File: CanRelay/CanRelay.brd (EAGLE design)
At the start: 93 x 65.5 mm, 21 parts

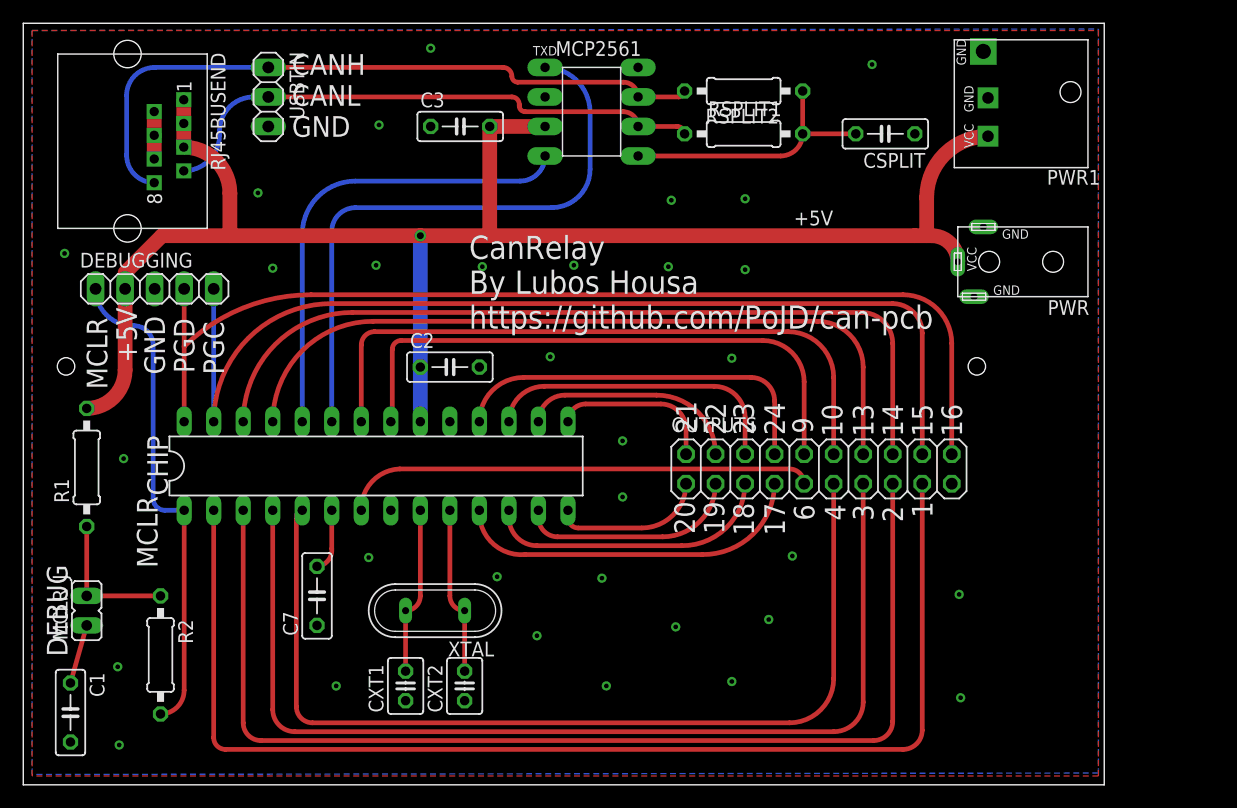
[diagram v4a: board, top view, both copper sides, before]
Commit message: #10 adding more missing GND vias to the board, running checks, adding  missing labels in schematic, done  #
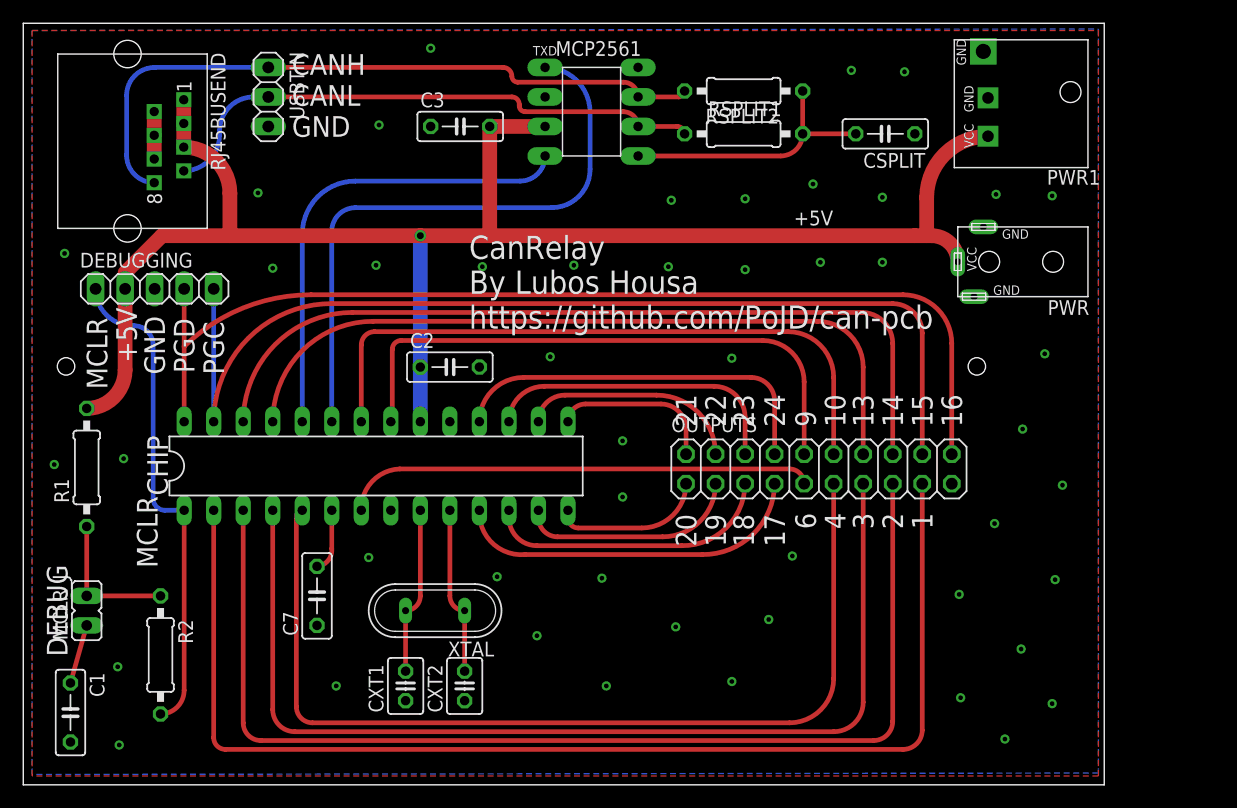
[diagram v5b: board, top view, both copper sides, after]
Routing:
- net GND: vias 32 -> 48
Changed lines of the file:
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@@
 <text x="17.272" y="35.306" size="1.778" layer="21" rot="R90">PGC</text>
 <text x="14.732" y="35.433" size="1.778" layer="21" rot="R90">PGD</text>
-<text x="57.912" y="30.226" size="1.778" layer="21" rot="R90">21</text>
-<text x="60.452" y="30.099" size="1.778" layer="21" rot="R90">22</text>
-<text x="62.865" y="30.099" size="1.778" layer="21" rot="R90">23</text>
-<text x="65.532" y="30.099" size="1.778" layer="21" rot="R90">24</text>
-<text x="67.945" y="30.226" size="1.778" layer="21" rot="R90">9</text>
-<text x="70.485" y="29.972" size="1.778" layer="21" rot="R90">10</text>
-<text x="73.152" y="29.972" size="1.778" layer="21" rot="R90">13</text>
-<text x="75.692" y="29.972" size="1.778" layer="21" rot="R90">14</text>
-<text x="78.232" y="29.972" size="1.778" layer="21" rot="R90">15</text>
-<text x="80.772" y="29.972" size="1.778" layer="21" rot="R90">16</text>
-<text x="57.785" y="21.59" size="1.778" layer="21" rot="R90">20</text>
-<text x="60.325" y="21.59" size="1.778" layer="21" rot="R90">19</text>
-<text x="62.865" y="21.463" size="1.778" layer="21" rot="R90">18</text>
-<text x="65.532" y="21.463" size="1.778" layer="21" rot="R90">17</text>
-<text x="68.072" y="22.733" size="1.778" layer="21" rot="R90">6</text>
-<text x="70.739" y="22.733" size="1.778" layer="21" rot="R90">4</text>
-<text x="73.152" y="22.733" size="1.778" layer="21" rot="R90">3</text>
-<text x="75.692" y="22.606" size="1.778" layer="21" rot="R90">2</text>
-<text x="78.232" y="22.987" size="1.778" layer="21" rot="R90">1</text>
+<text x="57.912" y="30.8" size="1.778" layer="21" rot="R90">21</text>
+<text x="60.452" y="30.8" size="1.778" layer="21" rot="R90">22</text>
+<text x="62.865" y="30.8" size="1.778" layer="21" rot="R90">23</text>
+<text x="65.532" y="30.8" size="1.778" layer="21" rot="R90">24</text>
+<text x="68.2" y="30.8" size="1.778" layer="21" rot="R90">9</text>
+<text x="70.739" y="30.8" size="1.778" layer="21" rot="R90">10</text>
+<text x="73.152" y="30.8" size="1.778" layer="21" rot="R90">13</text>
+<text x="75.692" y="30.8" size="1.778" layer="21" rot="R90">14</text>
+<text x="78.232" y="30.8" size="1.778" layer="21" rot="R90">15</text>
+<text x="80.772" y="30.8" size="1.778" layer="21" rot="R90">16</text>
+<text x="57.912" y="20.5" size="1.778" layer="21" rot="R90">20</text>
+<text x="60.452" y="20.5" size="1.778" layer="21" rot="R90">19</text>
+<text x="62.865" y="20.5" size="1.778" layer="21" rot="R90">18</text>
+<text x="65.532" y="20.5" size="1.778" layer="21" rot="R90">17</text>
+<text x="68.2" y="22" size="1.778" layer="21" rot="R90">6</text>
+<text x="70.739" y="22" size="1.778" layer="21" rot="R90">4</text>
+<text x="73.152" y="22" size="1.778" layer="21" rot="R90">3</text>
+<text x="75.692" y="22" size="1.778" layer="21" rot="R90">2</text>
+<text x="78.232" y="22" size="1.778" layer="21" rot="R90">1</text>
 <text x="11.557" y="18.669" size="1.778" layer="21" rot="R90">MCLR</text>
 <text x="3.81" y="11.049" size="1.778" layer="21" rot="R90">DEBUG</text>
@@
 <via x="3.556" y="45.72" extent="1-16" drill="0.4" shape="square"/>
 <via x="35.052" y="63.373" extent="1-16" drill="0.4" shape="square"/>
-<via x="73.025" y="61.976" extent="1-16" drill="0.4" shape="square"/>
+<via x="71.247" y="61.468" extent="1-16" drill="0.4" shape="square"/>
 <via x="8.636" y="28.067" extent="1-16" drill="0.4" shape="square"/>
 <via x="30.607" y="56.769" extent="1-16" drill="0.4" shape="square"/>
@@
 <wire x1="11.268" y1="57.922" x2="11.268" y2="55.882" width="1.27" layer="1"/>
 <wire x1="11.268" y1="55.882" x2="11.268" y2="53.842" width="1.27" layer="1"/>
+<via x="87.884" y="37.084" extent="1-16" drill="0.4" shape="square"/>
+<via x="85.979" y="30.607" extent="1-16" drill="0.4" shape="square"/>
+<via x="89.408" y="25.781" extent="1-16" drill="0.4" shape="square"/>
+<via x="83.566" y="22.479" extent="1-16" drill="0.4" shape="square"/>
+<via x="88.773" y="17.653" extent="1-16" drill="0.4" shape="square"/>
+<via x="85.852" y="11.684" extent="1-16" drill="0.4" shape="square"/>
+<via x="88.519" y="6.985" extent="1-16" drill="0.4" shape="square"/>
+<via x="84.455" y="3.937" extent="1-16" drill="0.4" shape="square"/>
+<via x="67.945" y="51.689" extent="1-16" drill="0.4" shape="square"/>
+<via x="73.914" y="50.546" extent="1-16" drill="0.4" shape="square"/>
+<via x="68.58" y="44.958" extent="1-16" drill="0.4" shape="square"/>
+<via x="73.914" y="44.958" extent="1-16" drill="0.4" shape="square"/>
+<via x="75.819" y="61.341" extent="1-16" drill="0.4" shape="square"/>
+<via x="2.667" y="27.559" extent="1-16" drill="0.4" shape="square"/>
+<via x="83.693" y="50.8" extent="1-16" drill="0.4" shape="square"/>
+<via x="88.519" y="50.673" extent="1-16" drill="0.4" shape="square"/>
 </signal>
 <signal name="N$2">

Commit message: #16 adding new FUSE component  - created before a new simple component from GME and added to schema  now  - wired up all, created new signal, used VCC for name and label +5V-RAW  - this is the actual power from the adapter, but FUSE would translate  that to +5V that all pins on the board use and need  - more tweaks and edits to make it all on the board  - labels and vias shuffled around too  - need to check the actual size of transceiver to make sure it can all  fit the board
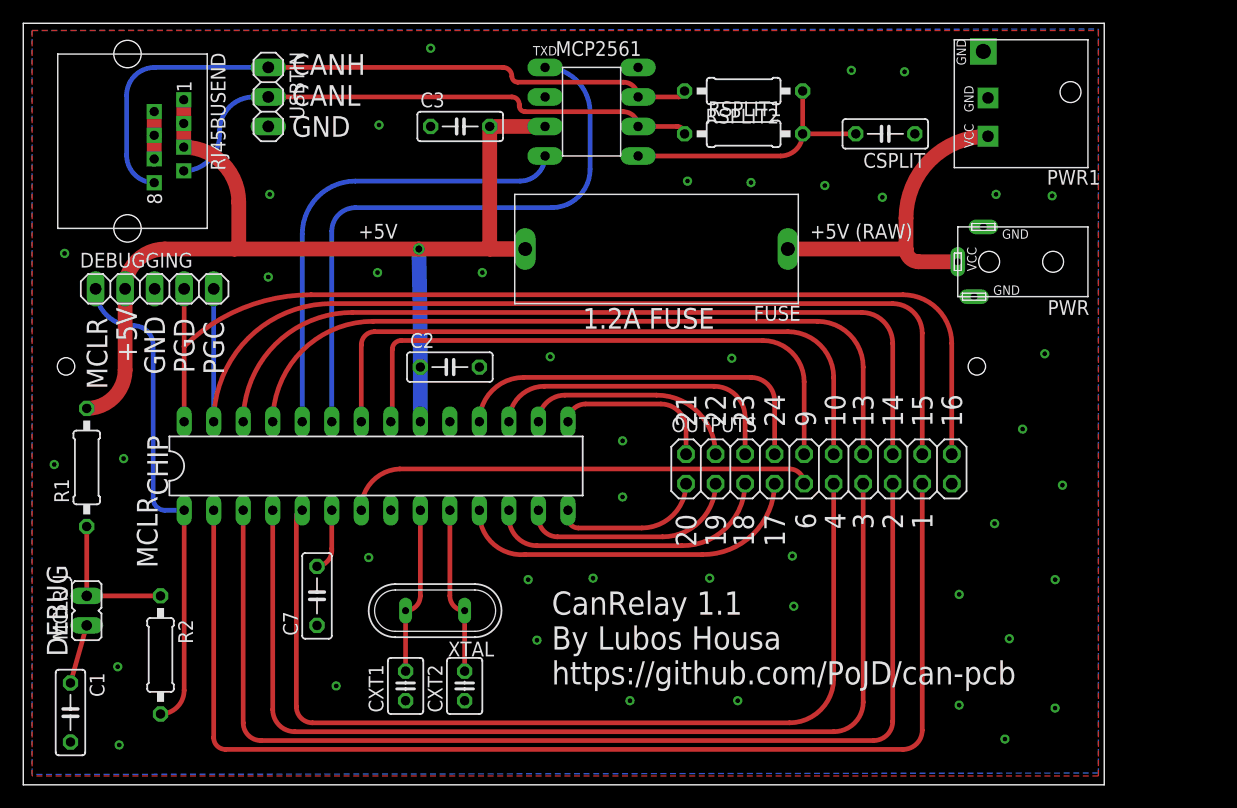
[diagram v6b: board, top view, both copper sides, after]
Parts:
- added FUSE: FUSE-PTF7878, PoJD:FUSE-PTF78
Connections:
- new net VCC: FUSE.P2, PWR.VCC, PWR1.VCC
- net +5V: now also FUSE.P1; no longer PWR.VCC, PWR1.VCC
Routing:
- net +5V: track 142.1 -> 96.6 mm
- net VCC: track 0.00 -> 27.7 mm
- net GND: vias 48 -> 43
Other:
- board text added: "+5V (RAW)"
- board text added: "1.2A FUSE"
- board text added: "CanRelay 1.1 By Lubos Housa https://github.com/PoJD/can-pcb"
- board text removed: "CanRelay By Lubos Housa https://github.com/PoJD/can-pcb"
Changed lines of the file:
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@@
 <wire x1="93" y1="65.522" x2="0" y2="65.522" width="0" layer="20"/>
 <wire x1="0" y1="65.522" x2="0" y2="0" width="0" layer="20"/>
-<text x="38.354" y="39.243" size="2" layer="21">CanRelay
+<text x="45.466" y="8.636" size="2" layer="21">CanRelay 1.1
 By Lubos Housa
 https://github.com/PoJD/can-pcb</text>
@@
 <text x="11.557" y="18.669" size="1.778" layer="21" rot="R90">MCLR</text>
 <text x="3.81" y="11.049" size="1.778" layer="21" rot="R90">DEBUG</text>
-<text x="66.294" y="48.133" size="1.27" layer="21">+5V</text>
+<text x="67.691" y="46.99" size="1.27" layer="21">+5V (RAW)</text>
+<text x="28.829" y="46.99" size="1.27" layer="21">+5V</text>
+<text x="48.133" y="39.243" size="1.778" layer="21">1.2A FUSE</text>
 </plain>
 <attributes>
@@
 <element name="USBTIN" library="pinhead" package="1X03" value="" x="21.082" y="59.182" rot="R270"/>
 <element name="PWR1" library="PoJD" package="DC-JACK-SCD-016A-2.5" value="DC-JACK-SCD-06A-2.5S" x="85.85" y="58.6" rot="R180"/>
+<element name="FUSE" library="PoJD" package="FUSE-PTF78" value="FUSE-PTF7878" x="54.483" y="46.101" rot="R180"/>
 </elements>
 <signals>
@@
 <contactref element="C3" pad="2"/>
 <contactref element="DEBUGGING" pad="2"/>
-<contactref element="PWR" pad="VCC"/>
-<wire x1="77.724" y1="47.244" x2="76.708" y2="47.244" width="1.27" layer="1"/>
-<wire x1="76.708" y1="47.244" x2="40.132" y2="47.244" width="1.27" layer="1"/>
-<wire x1="40.132" y1="47.244" x2="34.163" y2="47.244" width="1.27" layer="1"/>
 <wire x1="8.763" y1="41.783" x2="8.763" y2="42.672" width="0.4064" layer="1"/>
-<via x="34.163" y="47.244" extent="1-16" drill="0.6" shape="square"/>
-<wire x1="34.163" y1="47.244" x2="17.78" y2="47.244" width="1.27" layer="1"/>
-<wire x1="8.763" y1="44.069" x2="8.763" y2="42.672" width="0.4064" layer="1"/>
-<contactref element="PWR1" pad="VCC"/>
-<wire x1="77.724" y1="50.524" x2="77.724" y2="47.244" width="1.27" layer="1"/>
-<wire x1="40.132" y1="56.642" x2="40.132" y2="47.244" width="1.27" layer="1"/>
-<wire x1="77.724" y1="50.524" x2="83" y2="55.8" width="1.27" layer="1" curve="-90"/>
 <contactref element="RJ45BUSEND" pad="RJ45_1"/>
 <contactref element="RJ45BUSEND" pad="RJ45_3"/>
@@
 <wire x1="13.808" y1="58.942" x2="13.808" y2="56.902" width="1.27" layer="1"/>
 <wire x1="13.808" y1="56.902" x2="13.808" y2="54.862" width="1.27" layer="1"/>
-<wire x1="13.808" y1="54.862" x2="17.78" y2="50.89" width="1.27" layer="1" curve="-90"/>
-<wire x1="17.78" y1="50.89" x2="17.78" y2="47.244" width="1.27" layer="1"/>
-<wire x1="8.763" y1="44.069" x2="11.938" y2="47.244" width="1.27" layer="1"/>
-<wire x1="11.938" y1="47.244" x2="17.78" y2="47.244" width="1.27" layer="1"/>
 <wire x1="44.895" y1="56.642" x2="40.132" y2="56.642" width="1.27" layer="1"/>
 <wire x1="5.461" y1="32.385" x2="8.763" y2="35.687" width="1.27" layer="1" curve="90"/>
 <wire x1="8.763" y1="35.687" x2="8.763" y2="42.672" width="1.27" layer="1"/>
-<wire x1="34.163" y1="47.244" x2="34.163" y2="35.941" width="1.27" layer="16"/>
 <wire x1="34.163" y1="35.941" x2="34.163" y2="31.242" width="1.27" layer="16"/>
-<wire x1="80.4" y1="45" x2="78.156" y2="47.244" width="1.27" layer="1" curve="90"/>
-<wire x1="78.156" y1="47.244" x2="77.724" y2="47.244" width="1.27" layer="1"/>
+<contactref element="FUSE" pad="P1"/>
+<wire x1="43.183" y1="46.101" x2="34.036" y2="46.101" width="1.27" layer="1"/>
+<wire x1="34.036" y1="46.101" x2="18.161" y2="46.101" width="1.27" layer="1"/>
+<wire x1="18.161" y1="46.101" x2="12.192" y2="46.101" width="1.27" layer="1"/>
+<wire x1="13.808" y1="54.862" x2="18.542" y2="50.128" width="1.27" layer="1" curve="-90"/>
+<wire x1="18.542" y1="50.128" x2="18.542" y2="46.482" width="1.27" layer="1"/>
+<wire x1="8.763" y1="42.672" x2="12.192" y2="46.101" width="1.27" layer="1" curve="-90"/>
+<wire x1="18.542" y1="46.482" x2="18.161" y2="46.101" width="1.27" layer="1" curve="-90"/>
+<wire x1="43.183" y1="46.101" x2="40.132" y2="46.101" width="1.27" layer="1"/>
+<wire x1="40.132" y1="46.101" x2="40.132" y2="56.642" width="1.27" layer="1"/>
+<wire x1="34.163" y1="35.941" x2="34.036" y2="46.101" width="1.27" layer="16" curve="1.43232"/>
+<via x="34.036" y="46.101" extent="1-16" drill="0.6"/>
 </signal>
 <signal name="GND">
@@
 <via x="29.718" y="19.558" extent="1-16" drill="0.4" shape="square"/>
 <via x="66.167" y="19.685" extent="1-16" drill="0.4" shape="square"/>
-<via x="64.135" y="14.224" extent="1-16" drill="0.4" shape="square"/>
-<via x="60.96" y="8.89" extent="1-16" drill="0.4" shape="square"/>
-<via x="56.134" y="13.589" extent="1-16" drill="0.4" shape="square"/>
-<via x="49.784" y="17.78" extent="1-16" drill="0.4" shape="square"/>
-<via x="44.196" y="12.827" extent="1-16" drill="0.4" shape="square"/>
-<via x="50.165" y="8.509" extent="1-16" drill="0.4" shape="square"/>
+<via x="66.294" y="15.367" extent="1-16" drill="0.4" shape="square"/>
+<via x="61.468" y="7.239" extent="1-16" drill="0.4" shape="square"/>
+<via x="59.055" y="17.78" extent="1-16" drill="0.4" shape="square"/>
+<via x="49.022" y="17.78" extent="1-16" drill="0.4" shape="square"/>
+<via x="44.196" y="12.446" extent="1-16" drill="0.4" shape="square"/>
+<via x="52.197" y="7.239" extent="1-16" drill="0.4" shape="square"/>
 <via x="80.518" y="16.383" extent="1-16" drill="0.4" shape="square"/>
-<via x="80.645" y="7.493" extent="1-16" drill="0.4" shape="square"/>
+<via x="80.518" y="6.858" extent="1-16" drill="0.4" shape="square"/>
 <via x="51.562" y="29.591" extent="1-16" drill="0.4" shape="square"/>
 <via x="51.562" y="24.765" extent="1-16" drill="0.4" shape="square"/>
 <via x="45.339" y="36.83" extent="1-16" drill="0.4" shape="square"/>
 <via x="60.96" y="36.703" extent="1-16" drill="0.4" shape="square"/>
-<via x="62.103" y="50.419" extent="1-16" drill="0.4" shape="square"/>
-<via x="55.753" y="50.292" extent="1-16" drill="0.4" shape="square"/>
-<via x="20.193" y="50.927" extent="1-16" drill="0.4" shape="square"/>
+<via x="62.611" y="51.816" extent="1-16" drill="0.4" shape="square"/>
+<via x="57.15" y="51.943" extent="1-16" drill="0.4" shape="square"/>
+<via x="21.209" y="50.8" extent="1-16" drill="0.4" shape="square"/>
 <via x="3.556" y="45.72" extent="1-16" drill="0.4" shape="square"/>
 <via x="35.052" y="63.373" extent="1-16" drill="0.4" shape="square"/>
@@
 <via x="8.636" y="28.067" extent="1-16" drill="0.4" shape="square"/>
 <via x="30.607" y="56.769" extent="1-16" drill="0.4" shape="square"/>
-<via x="21.463" y="44.45" extent="1-16" drill="0.4" shape="square"/>
-<via x="62.103" y="44.323" extent="1-16" drill="0.4" shape="square"/>
-<via x="30.353" y="44.704" extent="1-16" drill="0.4" shape="square"/>
-<via x="39.497" y="44.577" extent="1-16" drill="0.4" shape="square"/>
-<via x="47.371" y="44.704" extent="1-16" drill="0.4" shape="square"/>
-<via x="55.499" y="44.577" extent="1-16" drill="0.4" shape="square"/>
-<via x="40.767" y="17.907" extent="1-16" drill="0.4" shape="square"/>
+<via x="21.082" y="43.688" extent="1-16" drill="0.4" shape="square"/>
+<via x="30.48" y="44.069" extent="1-16" drill="0.4" shape="square"/>
+<via x="39.497" y="44.069" extent="1-16" drill="0.4" shape="square"/>
+<via x="43.434" y="17.653" extent="1-16" drill="0.4" shape="square"/>
 <contactref element="PWR1" pad="GND2"/>
 <contactref element="PWR1" pad="GND1"/>
@@
 <via x="83.566" y="22.479" extent="1-16" drill="0.4" shape="square"/>
 <via x="88.773" y="17.653" extent="1-16" drill="0.4" shape="square"/>
-<via x="85.852" y="11.684" extent="1-16" drill="0.4" shape="square"/>
-<via x="88.519" y="6.985" extent="1-16" drill="0.4" shape="square"/>
+<via x="84.836" y="12.573" extent="1-16" drill="0.4" shape="square"/>
+<via x="88.773" y="6.604" extent="1-16" drill="0.4" shape="square"/>
 <via x="84.455" y="3.937" extent="1-16" drill="0.4" shape="square"/>
-<via x="67.945" y="51.689" extent="1-16" drill="0.4" shape="square"/>
+<via x="68.961" y="51.562" extent="1-16" drill="0.4" shape="square"/>
 <via x="73.914" y="50.546" extent="1-16" drill="0.4" shape="square"/>
-<via x="68.58" y="44.958" extent="1-16" drill="0.4" shape="square"/>
-<via x="73.914" y="44.958" extent="1-16" drill="0.4" shape="square"/>
 <via x="75.819" y="61.341" extent="1-16" drill="0.4" shape="square"/>
 <via x="2.667" y="27.559" extent="1-16" drill="0.4" shape="square"/>
@@
 <wire x1="46.863" y1="22.987" x2="46.863" y2="23.622" width="0.4064" layer="1"/>
 </signal>
+<signal name="VCC">
+<contactref element="PWR" pad="VCC"/>
+<contactref element="PWR1" pad="VCC"/>
+<contactref element="FUSE" pad="P2"/>
+<wire x1="65.783" y1="46.101" x2="75.946" y2="46.101" width="1.27" layer="1"/>
+<wire x1="75.946" y1="46.101" x2="77.047" y2="45" width="1.27" layer="1" curve="90"/>
+<wire x1="75.946" y1="48.746" x2="75.946" y2="46.101" width="1.27" layer="1"/>
+<wire x1="77.047" y1="45" x2="80.4" y2="45" width="1.27" layer="1"/>
+<wire x1="75.946" y1="48.746" x2="83" y2="55.8" width="1.27" layer="1" curve="-90"/>
+</signal>
 </signals>
